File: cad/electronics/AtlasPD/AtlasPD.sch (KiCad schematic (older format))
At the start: 12 parts, among them J1 Conn_01x02_Male, J2 Conn_01x02_Male, U1 LM2678T-ADJ_NOPB

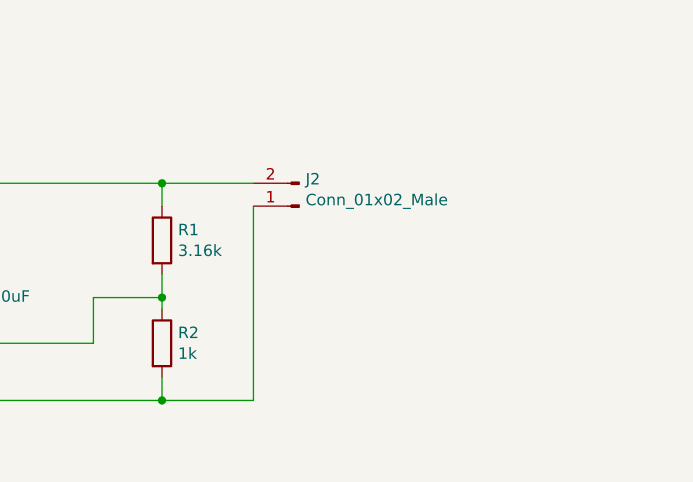
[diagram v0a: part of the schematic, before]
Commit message: Finished Basic Buck Converter Design
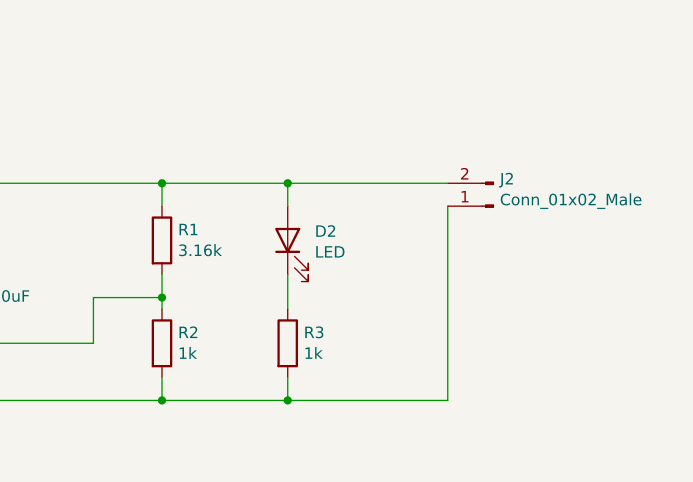
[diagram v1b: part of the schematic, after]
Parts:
- added D2: LED, LED_SMD:LED_0805_2012Metric, symbol Device:LED
- added R3: 1k, Resistor_SMD:R_0805_2012Metric, symbol Device:R
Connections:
- wire segments 44 -> 49
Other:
- moved on the sheet: J2
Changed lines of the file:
@@
 L Connector:Conn_01x02_Male J2
 U 1 1 605D0123
-P 8750 2550
-F 0 "J2" H 8722 2432 50  0000 R CNN
-F 1 "Conn_01x02_Male" H 8722 2523 50  0000 R CNN
-F 2 "Connector_PinHeader_2.54mm:PinHeader_1x02_P2.54mm_Vertical" H 8750 2550 50  0001 C CNN
-F 3 "~" H 8750 2550 50  0001 C CNN
-	1    8750 2550
+P 9600 2550
+F 0 "J2" H 9572 2432 50  0000 R CNN
+F 1 "Conn_01x02_Male" H 9572 2523 50  0000 R CNN
+F 2 "Connector_PinHeader_2.54mm:PinHeader_1x02_P2.54mm_Vertical" H 9600 2550 50  0001 C CNN
+F 3 "~" H 9600 2550 50  0001 C CNN
+	1    9600 2550
 	-1   0    0    1
 $EndComp
 Wire Wire Line
-	8150 2450 8550 2450
+	9400 2550 9400 3400
+$Comp
+L Device:R R3
+U 1 1 605D6524
+P 8700 3150
+F 0 "R3" H 8770 3196 50  0000 L CNN
+F 1 "1k" H 8770 3105 50  0000 L CNN
+F 2 "Resistor_SMD:R_0805_2012Metric" V 8630 3150 50  0001 C CNN
+F 3 "~" H 8700 3150 50  0001 C CNN
+	1    8700 3150
+	1    0    0    -1
+$EndComp
+$Comp
+L Device:LED D2
+U 1 1 605D69E6
+P 8700 2700
+F 0 "D2" V 8739 2582 50  0000 R CNN
+F 1 "LED" V 8648 2582 50  0000 R CNN
+F 2 "LED_SMD:LED_0805_2012Metric" H 8700 2700 50  0001 C CNN
+F 3 "~" H 8700 2700 50  0001 C CNN
+	1    8700 2700
+	0    -1   -1   0
+$EndComp
+Wire Wire Line
+	8150 2450 8700 2450
+Wire Wire Line
+	8700 2450 8700 2550
 Connection ~ 8150 2450
 Wire Wire Line
-	8550 2550 8550 3400
+	8700 2450 9400 2450
+Connection ~ 8700 2450
 Wire Wire Line
-	8550 3400 8150 3400
+	8700 2850 8700 3000
+Wire Wire Line
+	8700 3300 8700 3400
+Wire Wire Line
+	8700 3400 9400 3400
+Wire Wire Line
+	8700 3400 8150 3400
+Connection ~ 8700 3400
 Connection ~ 8150 3400
 $EndSCHEMATC

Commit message: Pushing latest changes
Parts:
- removed C1: 220uF, Capacitor_THT:CP_Radial_D5.0mm_P2.50mm, symbol Device:CP1
- removed C2, C3, C4: 10uF, Capacitor_SMD:C_0805_2012Metric, symbol Device:C
- removed C5: 1000uF, Capacitor_THT:CP_Radial_D5.0mm_P2.50mm, symbol Device:CP1
- removed D1: D_Schottky, Capacitor_SMD:C_0805_2012Metric, symbol Device:D_Schottky
- removed D2: LED, LED_SMD:LED_0805_2012Metric, symbol Device:LED
- removed J1, J2: Conn_01x02_Male, Connector_PinHeader_2.54mm:PinHeader_1x02_P2.54mm_Vertical, symbol Connector:Conn_01x02_Male
- removed L1: 22 uH, Inductor_THT:L_Axial_L6.6mm_D2.7mm_P10.16mm_Horizontal_Vishay_IM-2, symbol Device:L
- removed R1: 3.16k, Resistor_SMD:R_0805_2012Metric, symbol Device:R
- removed R2, R3: 1k, Resistor_SMD:R_0805_2012Metric, symbol Device:R
- removed U1: LM2678T-ADJ_NOPB, LM2678:TO127P1041X469X2199-7N, symbol LM2678T-ADJ/NOPB:LM2678T-ADJ_NOPB
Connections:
- net labels removed: GND
- wire segments 49 -> 0

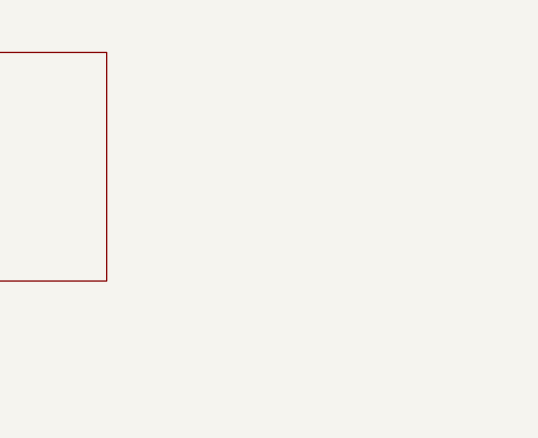
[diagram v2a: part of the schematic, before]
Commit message: Started adding ROS stuff to Arduino, Started Laying out Electrical Diagram
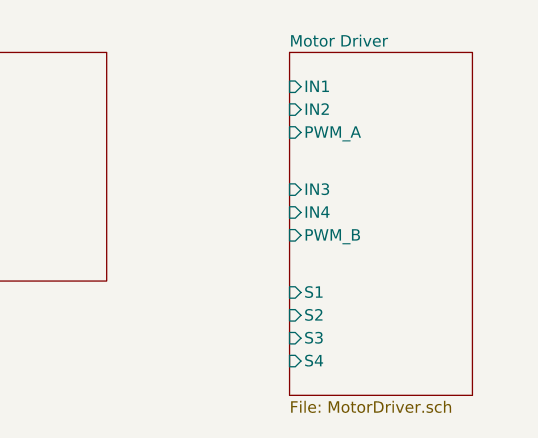
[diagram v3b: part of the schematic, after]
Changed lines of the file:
@@
 $Descr A4 11693 8268
 encoding utf-8
-Sheet 1 3
+Sheet 1 4
 Title ""
 Date ""
@@
 F1 "Microcontroller.sch" 50
 $EndSheet
+$Sheet
+S 6400 3750 800  1500
+U 6125CBA9
+F0 "Motor Driver" 50
+F1 "MotorDriver.sch" 50
+F2 "S1" I L 6400 4800 50
+F3 "S2" I L 6400 4900 50
+F4 "S3" I L 6400 5000 50
+F5 "S4" I L 6400 5100 50
+F6 "IN1" I L 6400 3900 50
+F7 "IN2" I L 6400 4000 50
+F8 "IN3" I L 6400 4350 50
+F9 "IN4" I L 6400 4450 50
+F10 "PWM_A" I L 6400 4100 50
+F11 "PWM_B" I L 6400 4550 50
+$EndSheet
 $EndSCHEMATC

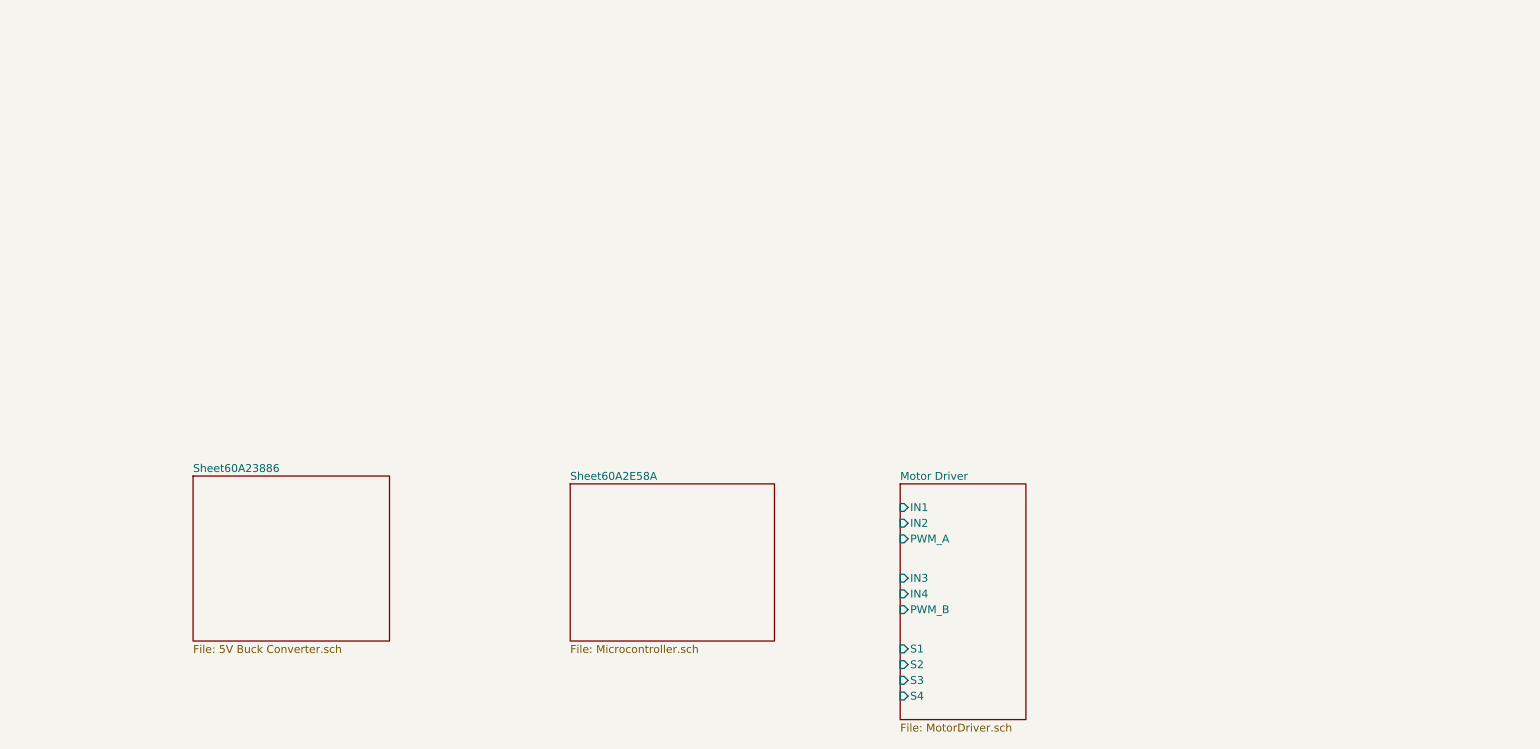
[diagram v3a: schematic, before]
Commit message: Added LDO
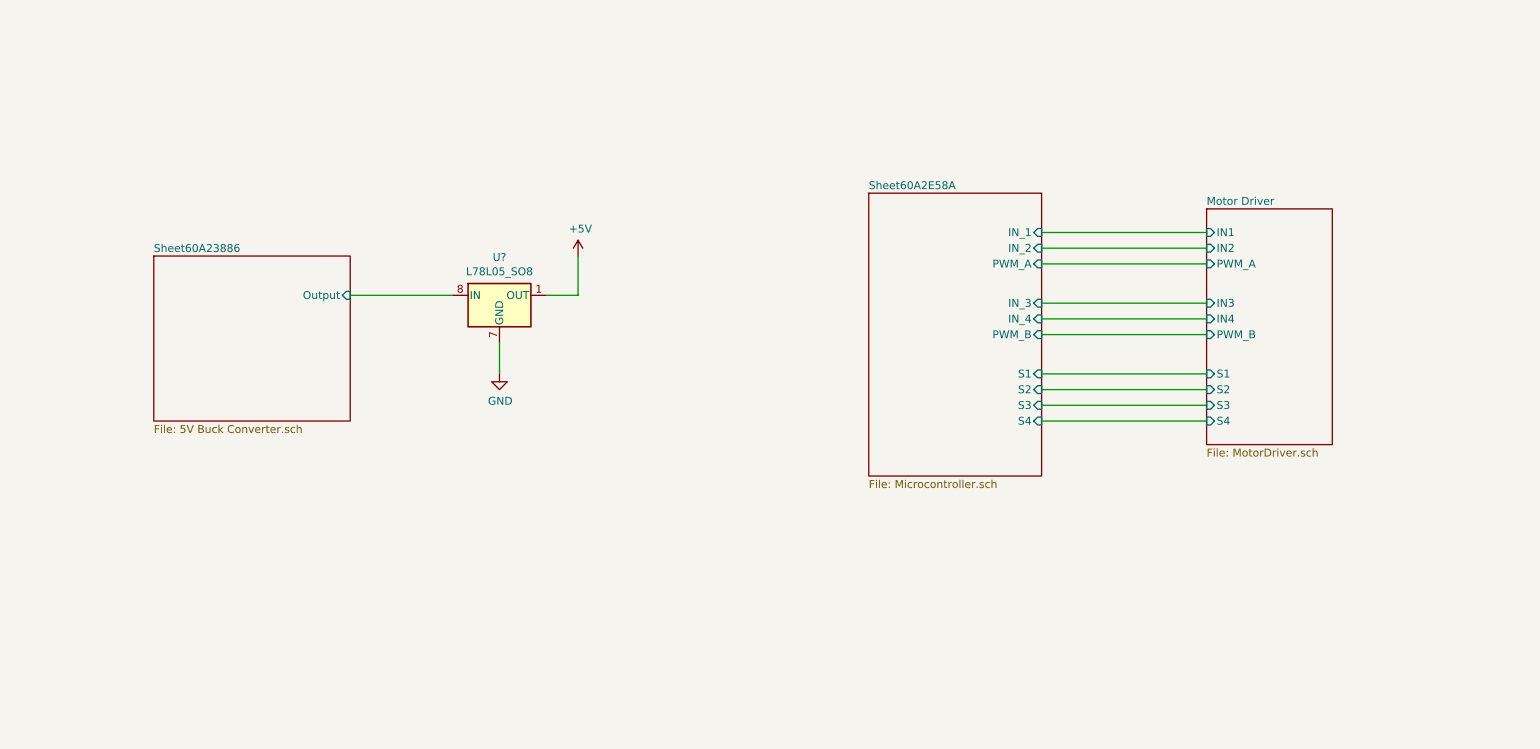
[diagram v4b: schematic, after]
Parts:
- added U?: L78L05_SO8, Package_SO:SOIC-8_3.9x4.9mm_P1.27mm, symbol Regulator_Linear:L78L05_SO8
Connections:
- new net +5V: U?.1 (OUT)
- new net GND: U?.2 (GND), U?.3 (GND), U?.6 (GND), U?.7 (GND)
- new net Sheet60A23886/Output: U?.8 (IN)
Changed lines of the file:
@@
 $EndDescr
 $Sheet
-S 1900 3700 1250 1050
+S 1650 2300 1250 1050
 U 60A23887
 F0 "Sheet60A23886" 50
 F1 "5V Buck Converter.sch" 50
+F2 "Output" I R 2900 2550 50
 $EndSheet
 $Sheet
-S 4300 3750 1300 1000
+S 6200 1900 1100 1800
 U 60A2E58B
 F0 "Sheet60A2E58A" 50
 F1 "Microcontroller.sch" 50
+F2 "IN_1" I R 7300 2150 50
+F3 "IN_2" I R 7300 2250 50
+F4 "PWM_A" I R 7300 2350 50
+F5 "IN_3" I R 7300 2600 50
+F6 "IN_4" I R 7300 2700 50
+F7 "PWM_B" I R 7300 2800 50
+F8 "S1" I R 7300 3050 50
+F9 "S2" I R 7300 3150 50
+F10 "S3" I R 7300 3250 50
+F11 "S4" I R 7300 3350 50
 $EndSheet
 $Sheet
-S 6400 3750 800  1500
+S 8350 2000 800  1500
 U 6125CBA9
 F0 "Motor Driver" 50
 F1 "MotorDriver.sch" 50
-F2 "S1" I L 6400 4800 50
-F3 "S2" I L 6400 4900 50
-F4 "S3" I L 6400 5000 50
-F5 "S4" I L 6400 5100 50
-F6 "IN1" I L 6400 3900 50
-F7 "IN2" I L 6400 4000 50
-F8 "IN3" I L 6400 4350 50
-F9 "IN4" I L 6400 4450 50
-F10 "PWM_A" I L 6400 4100 50
-F11 "PWM_B" I L 6400 4550 50
+F2 "S1" I L 8350 3050 50
+F3 "S2" I L 8350 3150 50
+F4 "S3" I L 8350 3250 50
+F5 "S4" I L 8350 3350 50
+F6 "IN1" I L 8350 2150 50
+F7 "IN2" I L 8350 2250 50
+F8 "IN3" I L 8350 2600 50
+F9 "IN4" I L 8350 2700 50
+F10 "PWM_A" I L 8350 2350 50
+F11 "PWM_B" I L 8350 2800 50
 $EndSheet
+Wire Wire Line
+	7300 2150 8350 2150
+Wire Wire Line
+	7300 2250 8350 2250
+Wire Wire Line
+	7300 2350 8350 2350
+Wire Wire Line
+	7300 2600 8350 2600
+Wire Wire Line
+	7300 2700 8350 2700
+Wire Wire Line
+	7300 2800 8350 2800
+Wire Wire Line
+	7300 3050 8350 3050
+Wire Wire Line
+	7300 3150 8350 3150
+Wire Wire Line
+	7300 3250 8350 3250
+Wire Wire Line
+	7300 3350 8350 3350
+$Comp
+L Regulator_Linear:L78L05_SO8 U?
+U 1 1 6141FB78
+P 3850 2550
+F 0 "U?" H 3850 2792 50  0000 C CNN
+F 1 "L78L05_SO8" H 3850 2701 50  0000 C CNN
+F 2 "Package_SO:SOIC-8_3.9x4.9mm_P1.27mm" H 3950 2750 50  0001 C CIN
+F 3 "http://www.st.com/content/ccc/resource/technical/document/datasheet/15/55/e5/aa/23/5b/43/fd/CD00000446.pdf/files/CD00000446.pdf/jcr:content/translations/en.CD00000446.pdf" H 4050 2550 50  0001 C CNN
+	1    3850 2550
+	1    0    0    -1
+$EndComp
+Wire Wire Line
+	2900 2550 3550 2550
+$Comp
+L power:+5V #PWR?
+U 1 1 61424002
+P 4350 2300
+F 0 "#PWR?" H 4350 2150 50  0001 C CNN
+F 1 "+5V" H 4365 2473 50  0000 C CNN
+F 2 "" H 4350 2300 50  0001 C CNN
+F 3 "" H 4350 2300 50  0001 C CNN
+	1    4350 2300
+	1    0    0    -1
+$EndComp
+Wire Wire Line
+	4350 2300 4350 2550
+Wire Wire Line
+	4350 2550 4150 2550
+$Comp
+L power:GND #PWR?
+U 1 1 614248BE
+P 3850 3050
+F 0 "#PWR?" H 3850 2800 50  0001 C CNN
+F 1 "GND" H 3855 2877 50  0000 C CNN
+F 2 "" H 3850 3050 50  0001 C CNN
+F 3 "" H 3850 3050 50  0001 C CNN
+	1    3850 3050
+	1    0    0    -1
+$EndComp
+Wire Wire Line
+	3850 2850 3850 3050
 $EndSCHEMATC

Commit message: Added part annotations
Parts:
- gave numbers to parts that had none: 1
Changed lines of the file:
@@
 	7300 3350 8350 3350
 $Comp
-L Regulator_Linear:L78L05_SO8 U?
+L Regulator_Linear:L78L05_SO8 U2
 U 1 1 6141FB78
 P 3850 2550
-F 0 "U?" H 3850 2792 50  0000 C CNN
+F 0 "U2" H 3850 2792 50  0000 C CNN
 F 1 "L78L05_SO8" H 3850 2701 50  0000 C CNN
 F 2 "Package_SO:SOIC-8_3.9x4.9mm_P1.27mm" H 3950 2750 50  0001 C CIN
@@
 	2900 2550 3550 2550
 $Comp
-L power:+5V #PWR?
+L power:+5V #PWR02
 U 1 1 61424002
 P 4350 2300
-F 0 "#PWR?" H 4350 2150 50  0001 C CNN
+F 0 "#PWR02" H 4350 2150 50  0001 C CNN
 F 1 "+5V" H 4365 2473 50  0000 C CNN
 F 2 "" H 4350 2300 50  0001 C CNN
@@
 	4350 2550 4150 2550
 $Comp
-L power:GND #PWR?
+L power:GND #PWR01
 U 1 1 614248BE
 P 3850 3050
-F 0 "#PWR?" H 3850 2800 50  0001 C CNN
+F 0 "#PWR01" H 3850 2800 50  0001 C CNN
 F 1 "GND" H 3855 2877 50  0000 C CNN
 F 2 "" H 3850 3050 50  0001 C CNN

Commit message: More Electronics design work
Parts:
- removed U2: L78L05_SO8, Package_SO:SOIC-8_3.9x4.9mm_P1.27mm, symbol Regulator_Linear:L78L05_SO8
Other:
- note added: "Buck Converter to convert \n+8V down to +5V/+3.3V"
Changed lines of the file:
@@
 $EndDescr
-$Sheet
-S 1650 2300 1250 1050
-U 60A23887
-F0 "Sheet60A23886" 50
-F1 "5V Buck Converter.sch" 50
-F2 "Output" I R 2900 2550 50
-$EndSheet
 $Sheet
 S 6200 1900 1100 1800
@@
 Wire Wire Line
 	7300 3350 8350 3350
-$Comp
-L Regulator_Linear:L78L05_SO8 U2
-U 1 1 6141FB78
-P 3850 2550
-F 0 "U2" H 3850 2792 50  0000 C CNN
-F 1 "L78L05_SO8" H 3850 2701 50  0000 C CNN
-F 2 "Package_SO:SOIC-8_3.9x4.9mm_P1.27mm" H 3950 2750 50  0001 C CIN
-F 3 "http://www.st.com/content/ccc/resource/technical/document/datasheet/15/55/e5/aa/23/5b/43/fd/CD00000446.pdf/files/CD00000446.pdf/jcr:content/translations/en.CD00000446.pdf" H 4050 2550 50  0001 C CNN
-	1    3850 2550
-	1    0    0    -1
-$EndComp
-Wire Wire Line
-	2900 2550 3550 2550
-$Comp
-L power:+5V #PWR02
-U 1 1 61424002
-P 4350 2300
-F 0 "#PWR02" H 4350 2150 50  0001 C CNN
-F 1 "+5V" H 4365 2473 50  0000 C CNN
-F 2 "" H 4350 2300 50  0001 C CNN
-F 3 "" H 4350 2300 50  0001 C CNN
-	1    4350 2300
-	1    0    0    -1
-$EndComp
-Wire Wire Line
-	4350 2300 4350 2550
-Wire Wire Line
-	4350 2550 4150 2550
-$Comp
-L power:GND #PWR01
-U 1 1 614248BE
-P 3850 3050
-F 0 "#PWR01" H 3850 2800 50  0001 C CNN
-F 1 "GND" H 3855 2877 50  0000 C CNN
-F 2 "" H 3850 3050 50  0001 C CNN
-F 3 "" H 3850 3050 50  0001 C CNN
-	1    3850 3050
-	1    0    0    -1
-$EndComp
-Wire Wire Line
-	3850 2850 3850 3050
+$Sheet
+S 1850 1400 1250 1050
+U 60A23887
+F0 "Sheet60A23886" 50
+F1 "5V Buck Converter.sch" 50
+$EndSheet
+Text Notes 1900 1600 0    50   ~ 0
+Buck Converter to convert \n+8V down to +5V/+3.3V
 $EndSCHEMATC

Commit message: Project Restructuring for ease of design and other stuff
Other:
- note added: "Encoder Feedback Signals\nFrom both motors"
- note added: "Motor 1 Control Signals"
- note added: "Motor 2 Control Signals"
- note added: "S1/S2: Motor 1\nS3/S4: Motor 2"
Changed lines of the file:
@@
 $EndDescr
 $Sheet
-S 6200 1900 1100 1800
+S 6950 1050 1100 1800
 U 60A2E58B
 F0 "Sheet60A2E58A" 50
 F1 "Microcontroller.sch" 50
-F2 "IN_1" I R 7300 2150 50
-F3 "IN_2" I R 7300 2250 50
-F4 "PWM_A" I R 7300 2350 50
-F5 "IN_3" I R 7300 2600 50
-F6 "IN_4" I R 7300 2700 50
-F7 "PWM_B" I R 7300 2800 50
-F8 "S1" I R 7300 3050 50
-F9 "S2" I R 7300 3150 50
-F10 "S3" I R 7300 3250 50
-F11 "S4" I R 7300 3350 50
+F2 "IN_1" I R 8050 1300 50
+F3 "IN_2" I R 8050 1400 50
+F4 "PWM_A" I R 8050 1500 50
+F5 "IN_3" I R 8050 1750 50
+F6 "IN_4" I R 8050 1850 50
+F7 "PWM_B" I R 8050 1950 50
+F8 "S1" I R 8050 2200 50
+F9 "S2" I R 8050 2300 50
+F10 "S3" I R 8050 2400 50
+F11 "S4" I R 8050 2500 50
 $EndSheet
 $Sheet
-S 8350 2000 800  1500
+S 9100 1150 800  1500
 U 6125CBA9
 F0 "Motor Driver" 50
 F1 "MotorDriver.sch" 50
-F2 "S1" I L 8350 3050 50
-F3 "S2" I L 8350 3150 50
-F4 "S3" I L 8350 3250 50
-F5 "S4" I L 8350 3350 50
-F6 "IN1" I L 8350 2150 50
-F7 "IN2" I L 8350 2250 50
-F8 "IN3" I L 8350 2600 50
-F9 "IN4" I L 8350 2700 50
-F10 "PWM_A" I L 8350 2350 50
-F11 "PWM_B" I L 8350 2800 50
+F2 "S1" I L 9100 2200 50
+F3 "S2" I L 9100 2300 50
+F4 "S3" I L 9100 2400 50
+F5 "S4" I L 9100 2500 50
+F6 "IN1" I L 9100 1300 50
+F7 "IN2" I L 9100 1400 50
+F8 "IN3" I L 9100 1750 50
+F9 "IN4" I L 9100 1850 50
+F10 "PWM_A" I L 9100 1500 50
+F11 "PWM_B" I L 9100 1950 50
 $EndSheet
 Wire Wire Line
-	7300 2150 8350 2150
+	8050 1300 9100 1300
 Wire Wire Line
-	7300 2250 8350 2250
+	8050 1400 9100 1400
 Wire Wire Line
-	7300 2350 8350 2350
+	8050 1500 9100 1500
 Wire Wire Line
-	7300 2600 8350 2600
+	8050 1750 9100 1750
 Wire Wire Line
-	7300 2700 8350 2700
+	8050 1850 9100 1850
 Wire Wire Line
-	7300 2800 8350 2800
+	8050 1950 9100 1950
 Wire Wire Line
-	7300 3050 8350 3050
+	8050 2200 9100 2200
 Wire Wire Line
-	7300 3150 8350 3150
+	8050 2300 9100 2300
 Wire Wire Line
-	7300 3250 8350 3250
+	8050 2400 9100 2400
 Wire Wire Line
-	7300 3350 8350 3350
+	8050 2500 9100 2500
 $Sheet
-S 1850 1400 1250 1050
+S 750  850  1250 1050
 U 60A23887
 F0 "Sheet60A23886" 50
 F1 "5V Buck Converter.sch" 50
 $EndSheet
-Text Notes 1900 1600 0    50   ~ 0
+Text Notes 800  1050 0    50   ~ 0
 Buck Converter to convert \n+8V down to +5V/+3.3V
+Text Notes 8100 1250 0    50   ~ 0
+Motor 1 Control Signals
+Text Notes 8100 1700 0    50   ~ 0
+Motor 2 Control Signals
+Text Notes 8100 2700 0    50   ~ 0
+Encoder Feedback Signals\nFrom both motors
+Text Notes 8100 2900 0    50   ~ 0
+S1/S2: Motor 1\nS3/S4: Motor 2
 $EndSCHEMATC

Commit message: Found a bug, squashed it
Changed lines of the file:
@@
 $EndSheet
 $Sheet
-S 9100 1150 800  1500
+S 9100 950  650  1800
 U 6125CBA9
 F0 "Motor Driver" 50
@@
 F10 "PWM_A" I L 9100 1500 50
 F11 "PWM_B" I L 9100 1950 50
+F12 "EN" I L 9100 1000 50
 $EndSheet
 Wire Wire Line
